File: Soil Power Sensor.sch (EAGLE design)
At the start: 99 parts, among them J1 12401832E402A, U10 TPS7A20330PDBVR, U11 TPS60403DBVR, U12 REF1933AIDDCR, U13 TLV1117LV33DCYR, U14 FSA2466UMX, U2 FT234XD-R, U3 MAX9944ATA+T, U4 ESP32-C3-MINI-1-N4, U5 LTC6362CDDPBF, U6 LTC6362CDDPBF, U7 INA296A5, U8 MAX11201AEUB+, U9 MAX11201AEUB+, X1 SMA-142-0701-801/806

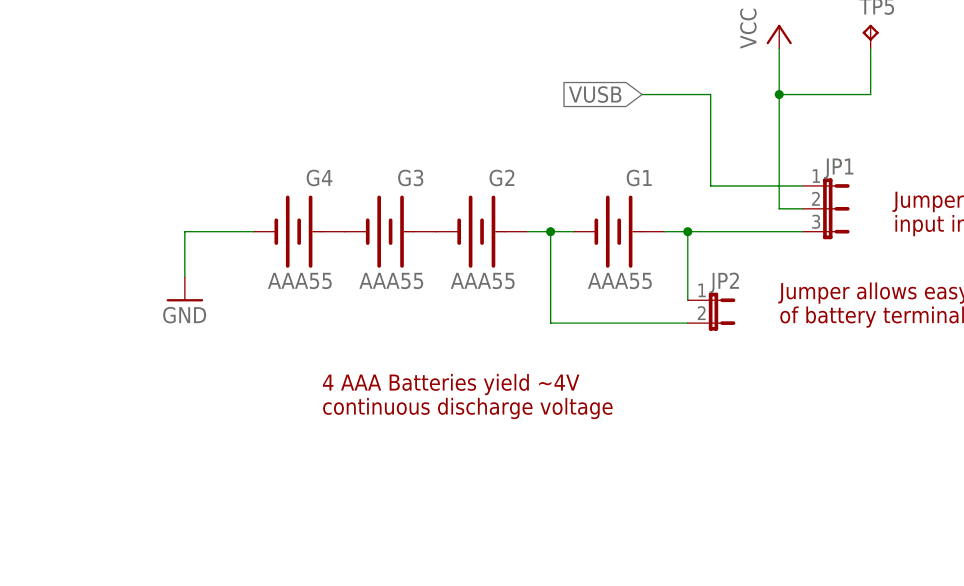
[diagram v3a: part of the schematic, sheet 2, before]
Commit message: Removed 4th battery jumper
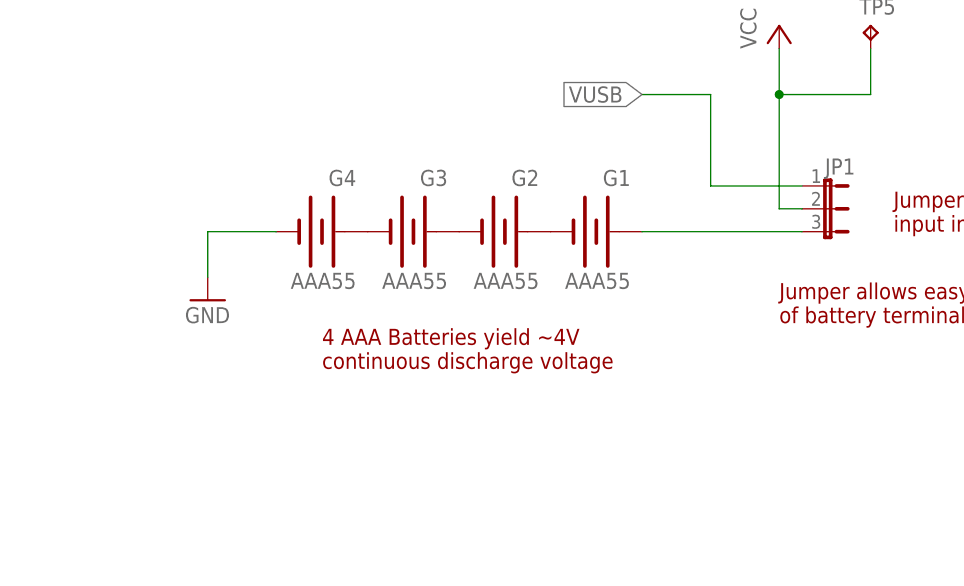
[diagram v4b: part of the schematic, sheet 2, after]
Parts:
- removed JP2: (no value), jumper:JP1E
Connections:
- net N$16: no longer JP2.2
- net N$19: no longer JP2.1
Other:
- moved on the sheet: G1, G2, G3, G4
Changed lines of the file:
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@@
 <part name="GND17" library="supply1" library_urn="urn:adsk.eagle:library:371" deviceset="GND" device=""/>
 <part name="P+3" library="supply1" library_urn="urn:adsk.eagle:library:371" deviceset="VCC" device=""/>
-<part name="JP2" library="jumper" library_urn="urn:adsk.eagle:library:252" deviceset="JP1E" device="" package3d_urn="urn:adsk.eagle:package:15455/1"/>
 <part name="FRAME4" library="frames" library_urn="urn:adsk.eagle:library:229" deviceset="FRAME_A_L" device=""/>
 <part name="U4" library="Soil Power Sensor" deviceset="ESP32-C3-MINI-1-N4" device=""/>
@@
 <text x="233.68" y="154.94" size="1.778" layer="94">Jumper for selecting
 input into Vcc</text>
-<text x="170.18" y="134.62" size="1.778" layer="94">4 AAA Batteries yield ~4V
+<text x="170.18" y="139.7" size="1.778" layer="94">4 AAA Batteries yield ~4V
 continuous discharge voltage</text>
 <text x="220.98" y="144.78" size="1.778" layer="94">Jumper allows easy bypass
@@
 <attribute name="VALUE" x="73.66" y="43.18" size="1.778" layer="96"/>
 </instance>
-<instance part="G1" gate="A" x="203.2" y="154.94" smashed="yes" rot="MR0">
-<attribute name="NAME" x="207.01" y="160.02" size="1.778" layer="95" rot="MR0"/>
-<attribute name="VALUE" x="207.01" y="148.59" size="1.778" layer="96" rot="MR0"/>
-</instance>
-<instance part="G2" gate="A" x="187.96" y="154.94" smashed="yes" rot="MR0">
-<attribute name="NAME" x="191.77" y="160.02" size="1.778" layer="95" rot="MR0"/>
-<attribute name="VALUE" x="191.77" y="148.59" size="1.778" layer="96" rot="MR0"/>
-</instance>
-<instance part="G3" gate="A" x="177.8" y="154.94" smashed="yes" rot="MR0">
-<attribute name="NAME" x="181.61" y="160.02" size="1.778" layer="95" rot="MR0"/>
-<attribute name="VALUE" x="181.61" y="148.59" size="1.778" layer="96" rot="MR0"/>
-</instance>
-<instance part="G4" gate="A" x="167.64" y="154.94" smashed="yes" rot="MR0">
-<attribute name="NAME" x="171.45" y="160.02" size="1.778" layer="95" rot="MR0"/>
-<attribute name="VALUE" x="171.45" y="148.59" size="1.778" layer="96" rot="MR0"/>
+<instance part="G1" gate="A" x="200.66" y="154.94" smashed="yes" rot="MR0">
+<attribute name="NAME" x="204.47" y="160.02" size="1.778" layer="95" rot="MR0"/>
+<attribute name="VALUE" x="204.47" y="148.59" size="1.778" layer="96" rot="MR0"/>
+</instance>
+<instance part="G2" gate="A" x="190.5" y="154.94" smashed="yes" rot="MR0">
+<attribute name="NAME" x="194.31" y="160.02" size="1.778" layer="95" rot="MR0"/>
+<attribute name="VALUE" x="194.31" y="148.59" size="1.778" layer="96" rot="MR0"/>
+</instance>
+<instance part="G3" gate="A" x="180.34" y="154.94" smashed="yes" rot="MR0">
+<attribute name="NAME" x="184.15" y="160.02" size="1.778" layer="95" rot="MR0"/>
+<attribute name="VALUE" x="184.15" y="148.59" size="1.778" layer="96" rot="MR0"/>
+</instance>
+<instance part="G4" gate="A" x="170.18" y="154.94" smashed="yes" rot="MR0">
+<attribute name="NAME" x="173.99" y="160.02" size="1.778" layer="95" rot="MR0"/>
+<attribute name="VALUE" x="173.99" y="148.59" size="1.778" layer="96" rot="MR0"/>
 </instance>
 <instance part="JP1" gate="1" x="226.06" y="157.48" smashed="yes" rot="R270">
@@
 <attribute name="VALUE" x="226.06" y="151.765" size="1.778" layer="96"/>
 </instance>
-<instance part="GND17" gate="1" x="154.94" y="147.32" smashed="yes">
-<attribute name="VALUE" x="152.4" y="144.78" size="1.778" layer="96"/>
+<instance part="GND17" gate="1" x="157.48" y="147.32" smashed="yes">
+<attribute name="VALUE" x="154.94" y="144.78" size="1.778" layer="96"/>
 </instance>
 <instance part="P+3" gate="VCC" x="220.98" y="177.8" smashed="yes">
 <attribute name="VALUE" x="218.44" y="175.26" size="1.778" layer="96" rot="R90"/>
-</instance>
-<instance part="JP2" gate="A" x="213.36" y="147.32" smashed="yes" rot="R270">
-<attribute name="NAME" x="213.36" y="148.59" size="1.778" layer="95"/>
-<attribute name="VALUE" x="213.36" y="141.605" size="1.778" layer="96"/>
 </instance>
 <instance part="TP1" gate="G$1" x="114.3" y="177.8" smashed="yes">
@@
 <pinref part="GND17" gate="1" pin="GND"/>
 <pinref part="G4" gate="A" pin="-"/>
-<wire x1="154.94" y1="149.86" x2="154.94" y2="154.94" width="0.1524" layer="91"/>
-<wire x1="154.94" y1="154.94" x2="162.56" y2="154.94" width="0.1524" layer="91"/>
+<wire x1="157.48" y1="149.86" x2="157.48" y2="154.94" width="0.1524" layer="91"/>
+<wire x1="157.48" y1="154.94" x2="165.1" y2="154.94" width="0.1524" layer="91"/>
 </segment>
 </net>
@@
 <pinref part="G1" gate="A" pin="-"/>
 <pinref part="G2" gate="A" pin="+"/>
-<wire x1="198.12" y1="154.94" x2="195.58" y2="154.94" width="0.1524" layer="91"/>
-<pinref part="JP2" gate="A" pin="2"/>
-<wire x1="195.58" y1="154.94" x2="193.04" y2="154.94" width="0.1524" layer="91"/>
-<wire x1="195.58" y1="154.94" x2="195.58" y2="144.78" width="0.1524" layer="91"/>
-<wire x1="195.58" y1="144.78" x2="210.82" y2="144.78" width="0.1524" layer="91"/>
-<junction x="195.58" y="154.94"/>
 </segment>
 </net>
@@
 <pinref part="G1" gate="A" pin="+"/>
 <pinref part="JP1" gate="1" pin="3"/>
-<wire x1="208.28" y1="154.94" x2="210.82" y2="154.94" width="0.1524" layer="91"/>
-<pinref part="JP2" gate="A" pin="1"/>
-<wire x1="210.82" y1="154.94" x2="223.52" y2="154.94" width="0.1524" layer="91"/>
-<wire x1="210.82" y1="147.32" x2="210.82" y2="154.94" width="0.1524" layer="91"/>
-<junction x="210.82" y="154.94"/>
-</segment>
-</net>
+<wire x1="205.74" y1="154.94" x2="223.52" y2="154.94" width="0.1524" layer="91"/>
+</segment>
+</net>

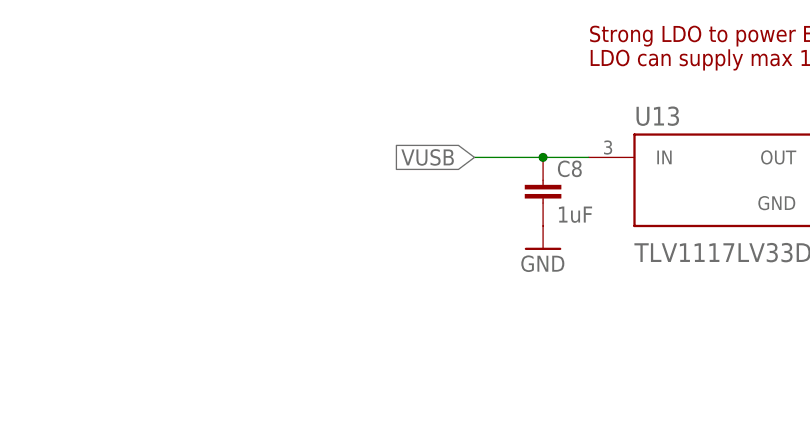
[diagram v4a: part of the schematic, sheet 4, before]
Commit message: Added jumper for selecting supply for ESP32
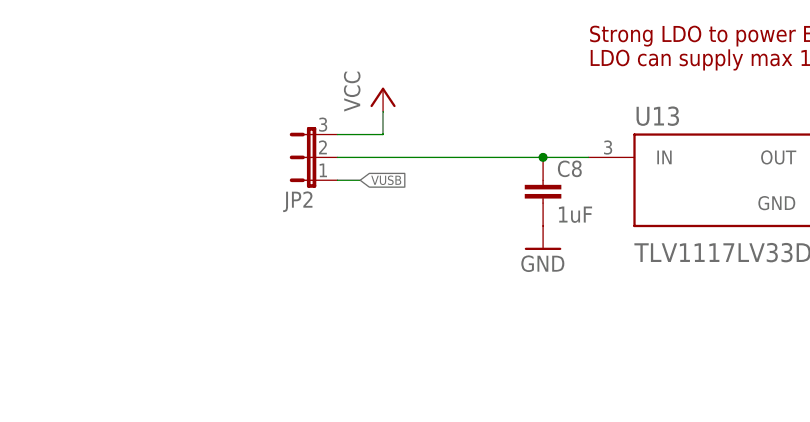
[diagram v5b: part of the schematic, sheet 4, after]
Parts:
- added JP2: (no value), jumper:JP2E
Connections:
- new net N$5: C8.1, JP2.2, U13.IN
- net VCC: now also JP2.3
- net VUSB: now also JP2.1; no longer C8.1, U13.IN
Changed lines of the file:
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@@
 <part name="I" library="con-wago-500" library_urn="urn:adsk.eagle:library:195" deviceset="W237-102" device="" package3d_urn="urn:adsk.eagle:package:10688/1"/>
 <part name="JP8" library="jumper" library_urn="urn:adsk.eagle:library:252" deviceset="JP1E" device="" package3d_urn="urn:adsk.eagle:package:15455/1"/>
+<part name="JP2" library="jumper" library_urn="urn:adsk.eagle:library:252" deviceset="JP2E" device="" package3d_urn="urn:adsk.eagle:package:15452/1"/>
+<part name="P+7" library="supply1" library_urn="urn:adsk.eagle:library:371" deviceset="VCC" device=""/>
 </parts>
 <sheets>
@@
 <attribute name="VALUE" x="66.04" y="22.86" size="1.778" layer="96"/>
 </instance>
+<instance part="JP2" gate="1" x="91.44" y="185.42" smashed="yes" rot="R90">
+<attribute name="NAME" x="91.44" y="181.61" size="1.778" layer="95" rot="R180"/>
+<attribute name="VALUE" x="91.44" y="191.135" size="1.778" layer="96" rot="R180"/>
+</instance>
+<instance part="P+7" gate="VCC" x="99.06" y="193.04" smashed="yes">
+<attribute name="VALUE" x="96.52" y="190.5" size="1.778" layer="96" rot="R90"/>
+</instance>
 </instances>
 <busses>
@@
 </segment>
 </net>
-<net name="VUSB" class="0">
-<segment>
-<pinref part="U13" gate="G$1" pin="IN"/>
-<label x="109.22" y="185.42" size="1.778" layer="95" rot="R180" xref="yes"/>
-<wire x1="121.92" y1="185.42" x2="116.84" y2="185.42" width="0.1524" layer="91"/>
-<pinref part="C8" gate="G$1" pin="1"/>
-<wire x1="116.84" y1="185.42" x2="109.22" y2="185.42" width="0.1524" layer="91"/>
-<junction x="116.84" y="185.42"/>
-</segment>
-</net>
 <net name="VUSB_3V3" class="0">
 <segment>
@@
 </segment>
 </net>
+<net name="N$5" class="0">
+<segment>
+<pinref part="U13" gate="G$1" pin="IN"/>
+<pinref part="C8" gate="G$1" pin="1"/>
+<wire x1="121.92" y1="185.42" x2="116.84" y2="185.42" width="0.1524" layer="91"/>
+<pinref part="JP2" gate="1" pin="2"/>
+<wire x1="93.98" y1="185.42" x2="116.84" y2="185.42" width="0.1524" layer="91"/>
+<junction x="116.84" y="185.42"/>
+</segment>
+</net>
+<net name="VUSB" class="0">
+<segment>
+<pinref part="JP2" gate="1" pin="1"/>
+<wire x1="93.98" y1="182.88" x2="96.52" y2="182.88" width="0.1524" layer="91"/>
+<label x="96.52" y="182.88" size="1.016" layer="95" xref="yes"/>
+</segment>
+</net>
+<net name="VCC" class="0">
+<segment>
+<pinref part="JP2" gate="1" pin="3"/>
+<pinref part="P+7" gate="VCC" pin="VCC"/>
+<wire x1="93.98" y1="187.96" x2="99.06" y2="187.96" width="0.1524" layer="91"/>
+<wire x1="99.06" y1="187.96" x2="99.06" y2="190.5" width="0.1524" layer="91"/>
+</segment>
+</net>
